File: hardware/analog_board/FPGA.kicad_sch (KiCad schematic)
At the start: 12 parts, among them U1 GW2A-LV18EQ144

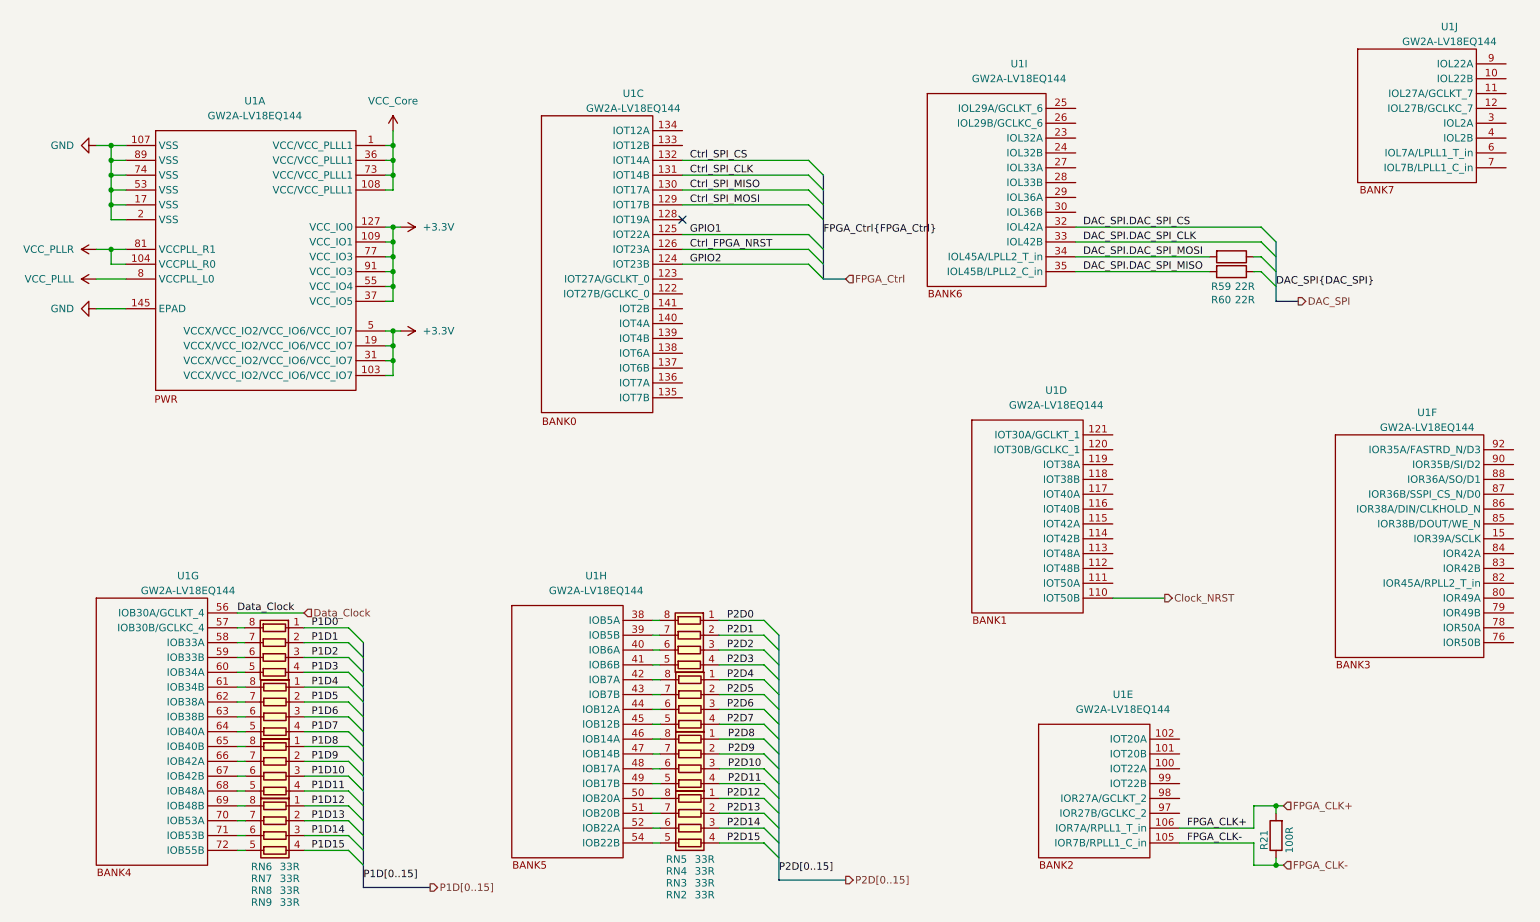
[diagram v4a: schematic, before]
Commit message: feat：模拟板电源 原理图设计
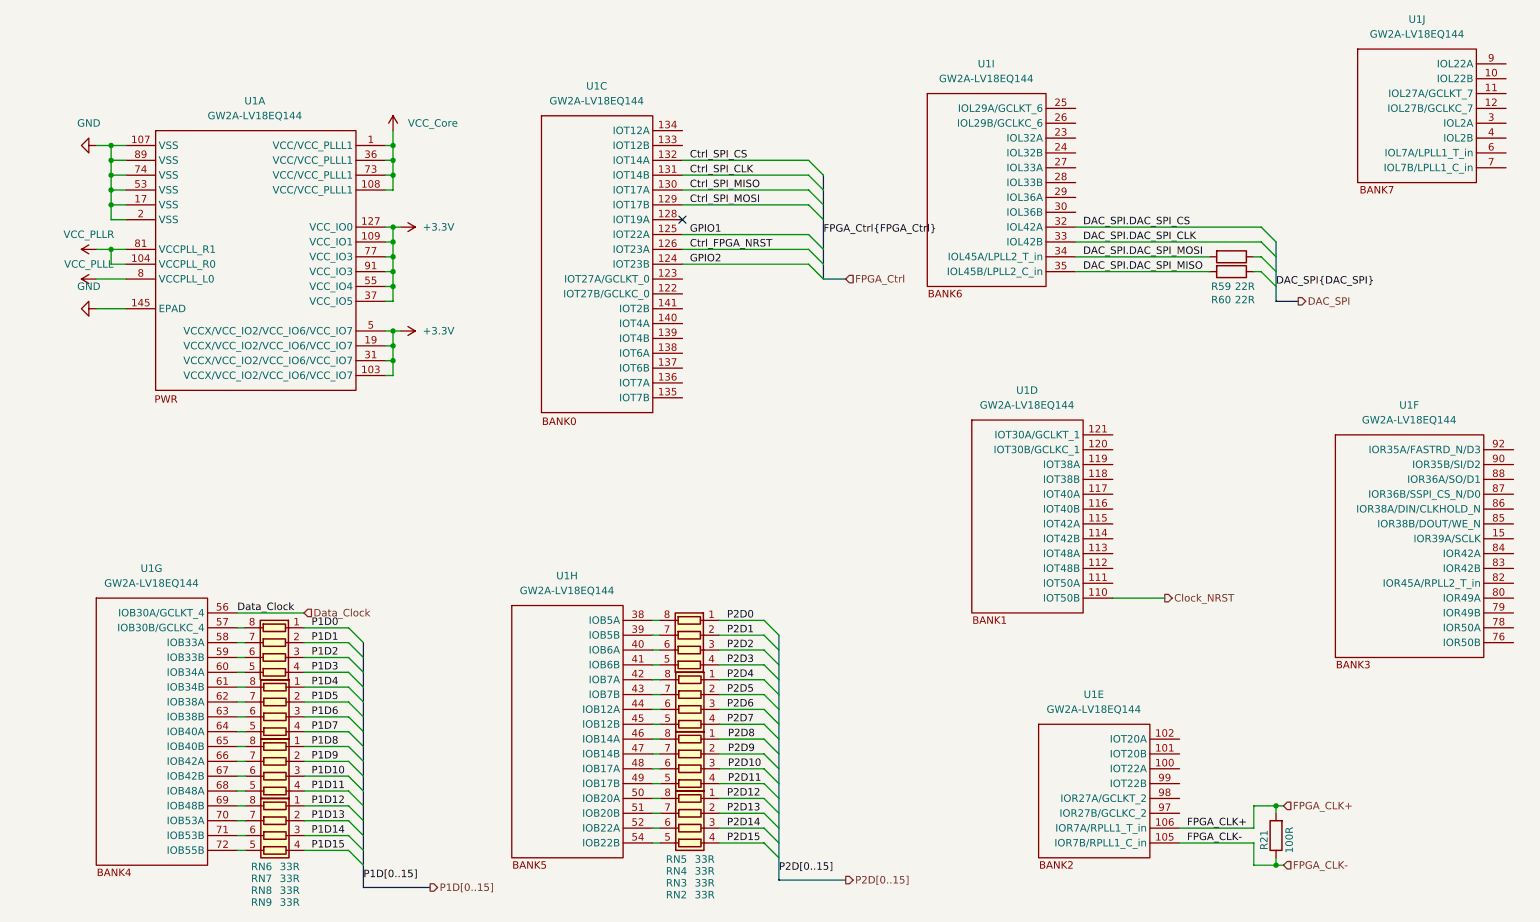
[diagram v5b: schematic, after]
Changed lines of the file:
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@@
 		)
 		(property "Value" "VCC_Core"
-			(at 88.9 29.21 0)
+			(at 91.44 33.0199 0)
 			(show_name no)
 			(do_not_autoplace no)
@@
 					(size 1.27 1.27)
 				)
+				(justify left)
 			)
 		)
@@
 		)
 		(property "Value" "VCC_PLLL"
-			(at 34.29 59.6899 90)
+			(at 36.83 57.15 90)
 			(show_name no)
 			(do_not_autoplace no)
@@
 					(size 1.27 1.27)
 				)
-				(justify left)
 			)
 		)
@@
 		(fields_autoplaced yes)
 		(property "Reference" "U1"
-			(at 213.8305 130.81 0)
+			(at 208.8412 130.81 0)
 			(show_name no)
 			(do_not_autoplace no)
@@
 		)
 		(property "Value" "GW2A-LV18EQ144"
-			(at 213.8305 133.35 0)
+			(at 208.8412 133.35 0)
 			(show_name no)
 			(do_not_autoplace no)
@@
 		(fields_autoplaced yes)
 		(property "Reference" "U1"
-			(at 202.4005 78.74 0)
+			(at 197.4112 78.74 0)
 			(show_name no)
 			(do_not_autoplace no)
@@
 		)
 		(property "Value" "GW2A-LV18EQ144"
-			(at 202.4005 81.28 0)
+			(at 197.4112 81.28 0)
 			(show_name no)
 			(do_not_autoplace no)
@@
 		(fields_autoplaced yes)
 		(property "Reference" "U1"
-			(at 123.6605 110.49 0)
+			(at 118.6712 110.49 0)
 			(show_name no)
 			(do_not_autoplace no)
@@
 		)
 		(property "Value" "GW2A-LV18EQ144"
-			(at 123.6605 113.03 0)
+			(at 118.6712 113.03 0)
 			(show_name no)
 			(do_not_autoplace no)
@@
 		(fields_autoplaced yes)
 		(property "Reference" "U1"
-			(at 265.9005 82.55 0)
+			(at 262.8162 81.28 0)
 			(show_name no)
 			(do_not_autoplace no)
@@
 		)
 		(property "Value" "GW2A-LV18EQ144"
-			(at 265.9005 85.09 0)
+			(at 262.8162 83.82 0)
 			(show_name no)
 			(do_not_autoplace no)
@@
 		(fields_autoplaced yes)
 		(property "Reference" "U1"
-			(at 53.8105 110.49 0)
+			(at 47.5512 109.22 0)
 			(show_name no)
 			(do_not_autoplace no)
@@
 		)
 		(property "Value" "GW2A-LV18EQ144"
-			(at 53.8105 113.03 0)
+			(at 47.5512 111.76 0)
 			(show_name no)
 			(do_not_autoplace no)
@@
 		)
 		(property "Value" "GND"
-			(at 34.29 36.8299 90)
+			(at 36.83 33.02 90)
 			(show_name no)
 			(do_not_autoplace no)
@@
 					(size 1.27 1.27)
 				)
-				(justify right)
 			)
 		)
@@
 		(fields_autoplaced yes)
 		(property "Reference" "U1"
-			(at 130.0105 27.94 0)
+			(at 123.7512 26.67 0)
 			(show_name no)
 			(do_not_autoplace no)
@@
 		)
 		(property "Value" "GW2A-LV18EQ144"
-			(at 130.0105 30.48 0)
+			(at 123.7512 29.21 0)
 			(show_name no)
 			(do_not_autoplace no)
@@
 		(fields_autoplaced yes)
 		(property "Reference" "U1"
-			(at 196.0505 22.86 0)
+			(at 190.4262 22.86 0)
 			(show_name no)
 			(do_not_autoplace no)
@@
 		)
 		(property "Value" "GW2A-LV18EQ144"
-			(at 196.0505 25.4 0)
+			(at 190.4262 25.4 0)
 			(show_name no)
 			(do_not_autoplace no)
@@
 		(fields_autoplaced yes)
 		(property "Reference" "U1"
-			(at 269.7105 16.51 0)
+			(at 264.16 15.24 0)
 			(show_name no)
 			(do_not_autoplace no)
@@
 		)
 		(property "Value" "GW2A-LV18EQ144"
-			(at 269.7105 19.05 0)
+			(at 264.16 17.78 0)
 			(show_name no)
 			(do_not_autoplace no)
@@
 		)
 		(property "Value" "GND"
-			(at 34.29 64.7699 90)
+			(at 36.83 60.96 90)
 			(show_name no)
 			(do_not_autoplace no)
@@
 					(size 1.27 1.27)
 				)
-				(justify right)
 			)
 		)
@@
 		)
 		(property "Value" "VCC_PLLR"
-			(at 34.29 54.6099 90)
+			(at 36.83 52.07 90)
 			(show_name no)
 			(do_not_autoplace no)
@@
 					(size 1.27 1.27)
 				)
-				(justify left)
 			)
 		)

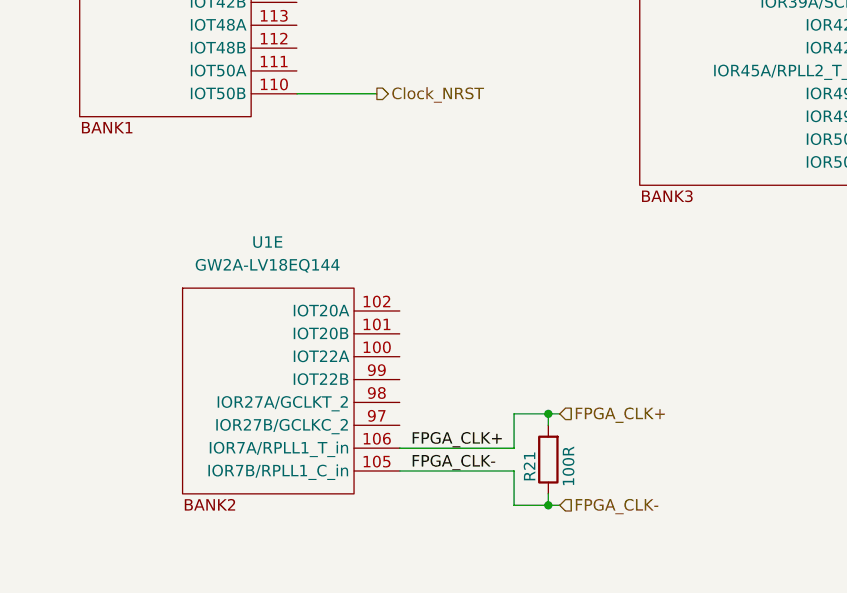
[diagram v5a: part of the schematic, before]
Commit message: feat：原理图添加测试点
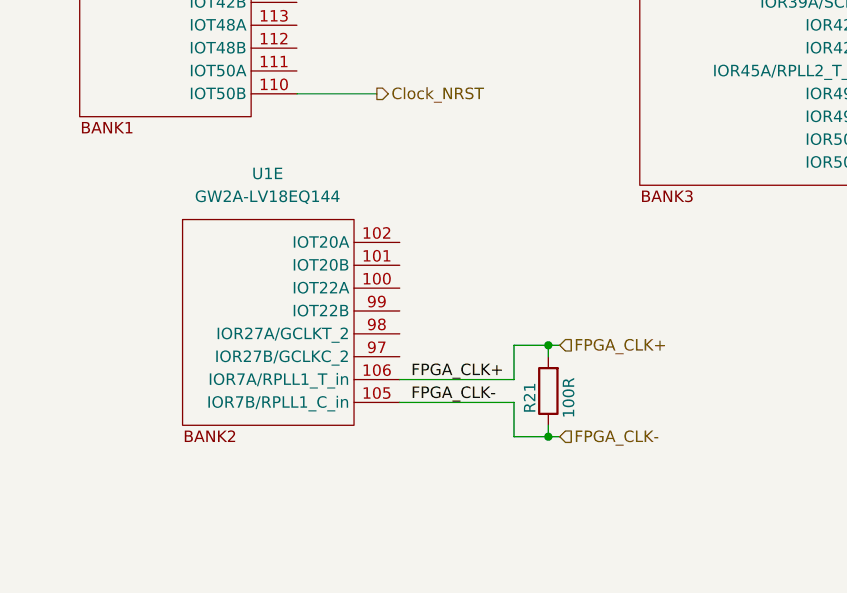
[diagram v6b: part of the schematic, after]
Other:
- moved on the sheet: R21, U1E
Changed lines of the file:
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@@
 	)
 	(junction
-		(at 240.03 160.02)
+		(at 240.03 152.4)
 		(diameter 0)
 		(color 0 0 0 0)
@@
 	)
 	(junction
-		(at 240.03 149.86)
+		(at 240.03 142.24)
 		(diameter 0)
 		(color 0 0 0 0)
@@
 	(wire
 		(pts
-			(xy 236.22 160.02) (xy 240.03 160.02)
+			(xy 236.22 152.4) (xy 240.03 152.4)
 		)
 		(stroke
@@
 	(wire
 		(pts
-			(xy 236.22 149.86) (xy 236.22 153.67)
+			(xy 236.22 142.24) (xy 236.22 146.05)
 		)
 		(stroke
@@
 	(wire
 		(pts
-			(xy 223.52 153.67) (xy 236.22 153.67)
+			(xy 223.52 146.05) (xy 236.22 146.05)
 		)
 		(stroke
@@
 	(wire
 		(pts
-			(xy 240.03 149.86) (xy 241.3 149.86)
-		)
-		(stroke
-			(width 0)
-			(type default)
-		)
-	)
-	(wire
-		(pts
-			(xy 240.03 158.75) (xy 240.03 160.02)
+			(xy 240.03 142.24) (xy 241.3 142.24)
+		)
+		(stroke
+			(width 0)
+			(type default)
+		)
+	)
+	(wire
+		(pts
+			(xy 240.03 151.13) (xy 240.03 152.4)
 		)
 		(stroke
@@
 	(wire
 		(pts
-			(xy 240.03 160.02) (xy 241.3 160.02)
+			(xy 240.03 152.4) (xy 241.3 152.4)
 		)
 		(stroke
@@
 	(wire
 		(pts
-			(xy 223.52 156.21) (xy 236.22 156.21)
+			(xy 223.52 148.59) (xy 236.22 148.59)
 		)
 		(stroke
@@
 	(wire
 		(pts
-			(xy 236.22 149.86) (xy 240.03 149.86)
+			(xy 236.22 142.24) (xy 240.03 142.24)
 		)
 		(stroke
@@
 	(wire
 		(pts
-			(xy 236.22 160.02) (xy 236.22 156.21)
+			(xy 236.22 152.4) (xy 236.22 148.59)
 		)
 		(stroke
@@
 	(wire
 		(pts
-			(xy 240.03 149.86) (xy 240.03 151.13)
+			(xy 240.03 142.24) (xy 240.03 143.51)
 		)
 		(stroke
@@
 	)
 	(label "FPGA_CLK-"
-		(at 224.79 156.21 0)
+		(at 224.79 148.59 0)
 		(effects
 			(font
@@
 	)
 	(label "FPGA_CLK+"
-		(at 224.79 153.67 0)
+		(at 224.79 146.05 0)
 		(effects
 			(font
@@
 	(hierarchical_label "FPGA_CLK-"
 		(shape input)
-		(at 241.3 160.02 0)
+		(at 241.3 152.4 0)
 		(effects
 			(font
@@
 	(hierarchical_label "FPGA_CLK+"
 		(shape input)
-		(at 241.3 149.86 0)
+		(at 241.3 142.24 0)
 		(effects
 			(font
@@
 	(symbol
 		(lib_id "Device:R")
-		(at 240.03 154.94 180)
+		(at 240.03 147.32 180)
 		(unit 1)
 		(body_style 1)
@@
 		(dnp no)
 		(property "Reference" "R21"
-			(at 237.998 155.702 90)
+			(at 237.998 148.082 90)
 			(show_name no)
 			(do_not_autoplace no)
@@
 		)
 		(property "Value" "100R"
-			(at 242.316 155.702 90)
+			(at 242.316 148.082 90)
 			(show_name no)
 			(do_not_autoplace no)
@@
 		)
 		(property "Footprint" "Resistor_SMD:R_0402_1005Metric"
-			(at 241.808 154.94 90)
+			(at 241.808 147.32 90)
 			(hide yes)
 			(show_name no)
@@
 		)
 		(property "Datasheet" ""
-			(at 240.03 154.94 0)
+			(at 240.03 147.32 0)
 			(hide yes)
 			(show_name no)
@@
 		)
 		(property "Description" "Resistor"
-			(at 240.03 154.94 0)
+			(at 240.03 147.32 0)
 			(hide yes)
 			(show_name no)
@@
 	(symbol
 		(lib_id "ArbWave30_lib:GW2AR-LV18EQ144C8/I7")
-		(at 195.58 132.08 0)
+		(at 195.58 124.46 0)
 		(unit 5)
 		(body_style 1)
@@
 		(fields_autoplaced yes)
 		(property "Reference" "U1"
-			(at 208.8412 130.81 0)
+			(at 208.8412 123.19 0)
 			(show_name no)
 			(do_not_autoplace no)
@@
 		)
 		(property "Value" "GW2A-LV18EQ144"
-			(at 208.8412 133.35 0)
+			(at 208.8412 125.73 0)
 			(show_name no)
 			(do_not_autoplace no)
@@
 		)
 		(property "Footprint" "ArbWave30_lib:LQFP-144_20x20_Pitch0.5mm"
-			(at 208.026 129.032 0)
+			(at 208.026 121.412 0)
 			(hide yes)
 			(show_name no)
@@
 		)
 		(property "Datasheet" ""
-			(at 195.58 132.08 0)
+			(at 195.58 124.46 0)
 			(hide yes)
 			(show_name no)
@@
 		)
 		(property "Description" ""
-			(at 195.58 132.08 0)
+			(at 195.58 124.46 0)
 			(hide yes)
 			(show_name no)

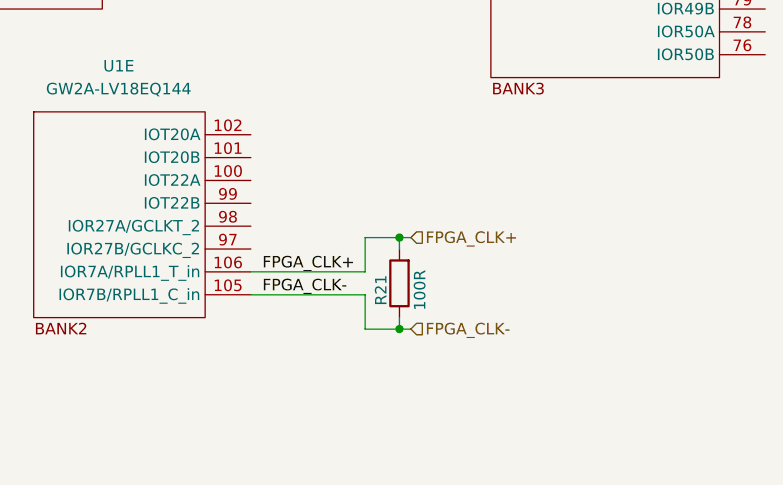
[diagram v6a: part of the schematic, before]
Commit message: feat：时钟电路预布局
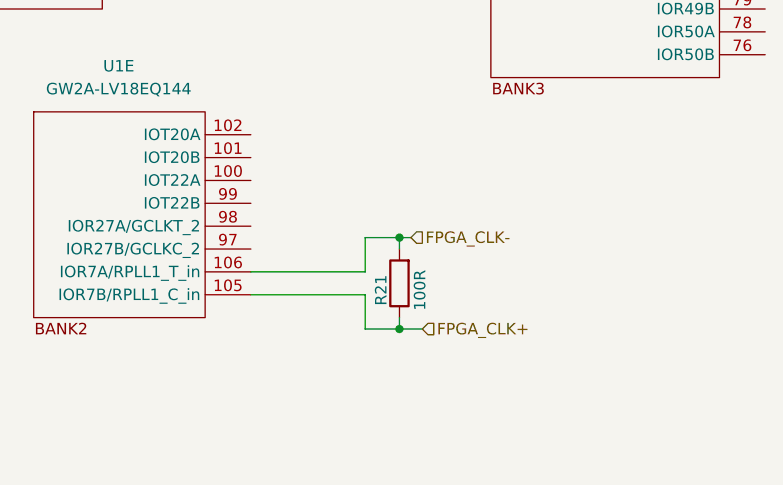
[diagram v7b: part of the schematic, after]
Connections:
- net FPGA_CLK+: now also R21.1, U1.105 (IOR7B/RPLL1_C_in); no longer R21.2, U1.106 (IOR7A/RPLL1_T_in)
- net FPGA_CLK-: now also R21.2, U1.106 (IOR7A/RPLL1_T_in); no longer R21.1, U1.105 (IOR7B/RPLL1_C_in)
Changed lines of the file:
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@@
+	)
+	(junction
+		(at 88.9 55.88)
+		(diameter 0)
+		(color 0 0 0 0)
+	)
+	(junction
+		(at 40.64 39.37)
+		(diameter 0)
+		(color 0 0 0 0)
+	)
+	(junction
+		(at 88.9 36.83)
+		(diameter 0)
+		(color 0 0 0 0)
+	)
+	(junction
+		(at 40.64 54.61)
+		(diameter 0)
+		(color 0 0 0 0)
+	)
+	(junction
+		(at 40.64 41.91)
+		(diameter 0)
+		(color 0 0 0 0)
+	)
+	(junction
+		(at 88.9 39.37)
+		(diameter 0)
+		(color 0 0 0 0)
+	)
+	(junction
+		(at 88.9 73.66)
+		(diameter 0)
+		(color 0 0 0 0)
+	)
+	(junction
+		(at 88.9 71.12)
+		(diameter 0)
+		(color 0 0 0 0)
+	)
+	(junction
+		(at 240.03 142.24)
+		(diameter 0)
+		(color 0 0 0 0)
+	)
+	(junction
+		(at 88.9 53.34)
+		(diameter 0)
+		(color 0 0 0 0)
+	)
+	(junction
+		(at 88.9 60.96)
+		(diameter 0)
+		(color 0 0 0 0)
 	)
 	(junction
@@
 	)
 	(junction
-		(at 88.9 55.88)
-		(diameter 0)
-		(color 0 0 0 0)
-	)
-	(junction
-		(at 40.64 39.37)
-		(diameter 0)
-		(color 0 0 0 0)
-	)
-	(junction
-		(at 88.9 36.83)
-		(diameter 0)
-		(color 0 0 0 0)
-	)
-	(junction
-		(at 40.64 54.61)
-		(diameter 0)
-		(color 0 0 0 0)
-	)
-	(junction
-		(at 40.64 41.91)
-		(diameter 0)
-		(color 0 0 0 0)
-	)
-	(junction
-		(at 88.9 39.37)
-		(diameter 0)
-		(color 0 0 0 0)
-	)
-	(junction
-		(at 88.9 73.66)
-		(diameter 0)
-		(color 0 0 0 0)
-	)
-	(junction
-		(at 88.9 71.12)
-		(diameter 0)
-		(color 0 0 0 0)
-	)
-	(junction
-		(at 240.03 142.24)
-		(diameter 0)
-		(color 0 0 0 0)
-	)
-	(junction
-		(at 88.9 53.34)
-		(diameter 0)
-		(color 0 0 0 0)
-	)
-	(junction
-		(at 88.9 60.96)
-		(diameter 0)
-		(color 0 0 0 0)
-	)
-	(junction
 		(at 88.9 68.58)
 		(diameter 0)
@@
 	(wire
 		(pts
-			(xy 240.03 152.4) (xy 241.3 152.4)
+			(xy 240.03 152.4) (xy 242.57 152.4)
 		)
 		(stroke
@@
 		)
 	)
-	(label "FPGA_CLK-"
-		(at 224.79 148.59 0)
-		(effects
-			(font
-				(size 1.27 1.27)
-			)
-			(justify left bottom)
-		)
-	)
 	(label "P2D12"
 		(at 146.05 148.59 0)
@@
 		)
 	)
-	(label "FPGA_CLK+"
-		(at 224.79 146.05 0)
-		(effects
-			(font
-				(size 1.27 1.27)
-			)
-			(justify left bottom)
-		)
-	)
 	(label "Ctrl_SPI_MISO"
 		(at 139.7 44.45 0)
@@
 	(hierarchical_label "FPGA_CLK-"
 		(shape input)
-		(at 241.3 152.4 0)
+		(at 241.3 142.24 0)
+		(effects
+			(font
+				(size 1.27 1.27)
+			)
+			(justify left)
+		)
+	)
+	(hierarchical_label "FPGA_CLK+"
+		(shape input)
+		(at 242.57 152.4 0)
 		(effects
 			(font
@@
 		(effects
 			(font
-				(size 1.27 1.27)
-			)
-			(justify left)
-		)
-	)
-	(hierarchical_label "FPGA_CLK+"
-		(shape input)
-		(at 241.3 142.24 0)
-		(effects
-			(font
